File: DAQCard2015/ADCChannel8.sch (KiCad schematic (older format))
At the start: 50 parts, among them U10 LTC6403, U6 LTC6403, U7 AD9219, U8 LTC6403, U9 LTC6403

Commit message: Replaces single ample with 4-channel varients. Greatly reducing part count
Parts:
- removed C23, C33, C37, C38: .01uF, symbol C
- removed C24, C25, C29, C31, C32: .1uF, symbol C
- removed C26, C27, C28, C34, C35, C36, C39, C40, C41: C, symbol C
- removed C30: 2.2uF, symbol CP
- removed R25: Rt, symbol R
- removed R26, R27, R39, R40, R41, R42: Ri, symbol R
- removed R29, R30, R43, R44, R45, R46: Rf, symbol R
- removed R31: 10k, symbol R
- removed R47: 2.7k, symbol R
- removed R48: 1k, symbol R
- removed U10, U6, U8, U9: LTC6403, symbol LTC6403
- removed U7: AD9219, symbol AD9219
- added C45: .01uF, symbol C
- added C46, C47, C48, C50, C51: .1uF, symbol C
- added C49: 2.2uF, symbol CP
- added RP13: R_PACK8, symbol R_PACK8
- added RP14, RP15: Rf, symbol R_PACK4
- added U10: THS4524IDBTR, symbol THS4524IDBTR
- added U11: AD9219, symbol AD9219
- R33, R34: value Ri -> Rt
- R35: value Rf -> Rt
- R36: value Rf -> 2.7k
- R37: value Rt -> 1k
- R38: value Rt -> 10k
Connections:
- net labels added: 3V3ana, VOCM
- net labels removed: 18ana, 3V3, Vocm
- wire segments 178 -> 192
- no-connect marks 12 -> 4
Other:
- note removed: "100R Termination \nis common for all ADCs."

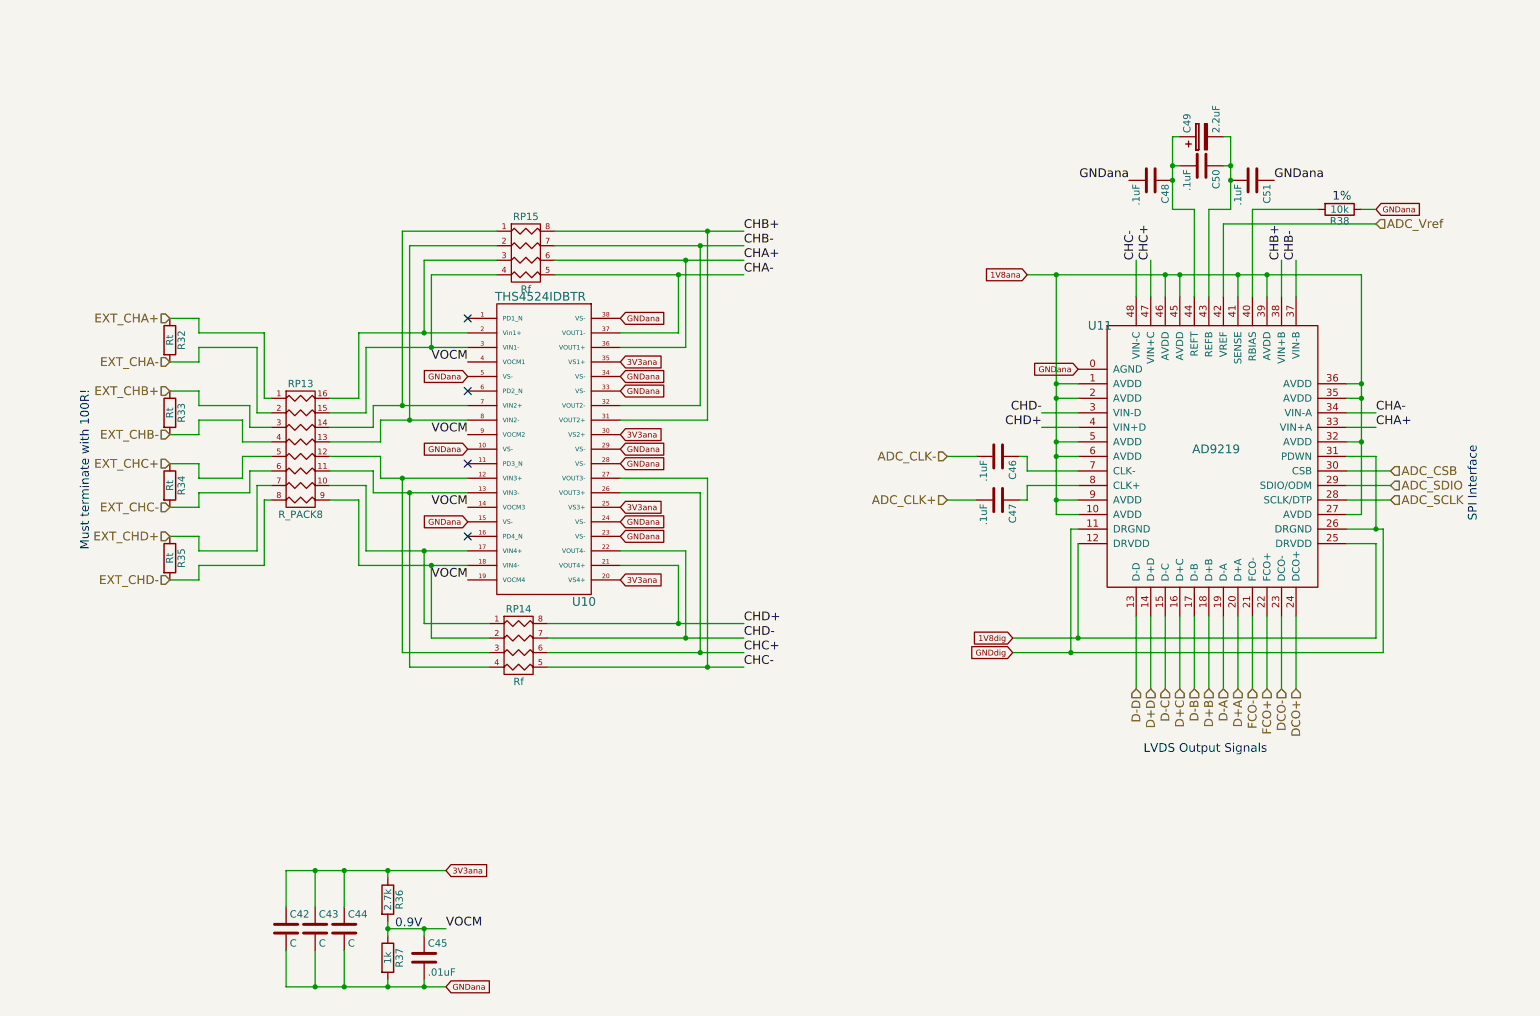
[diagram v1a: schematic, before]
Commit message: Finishes initial version of schematic(mostly). And adds a whole bunch of new footprints!
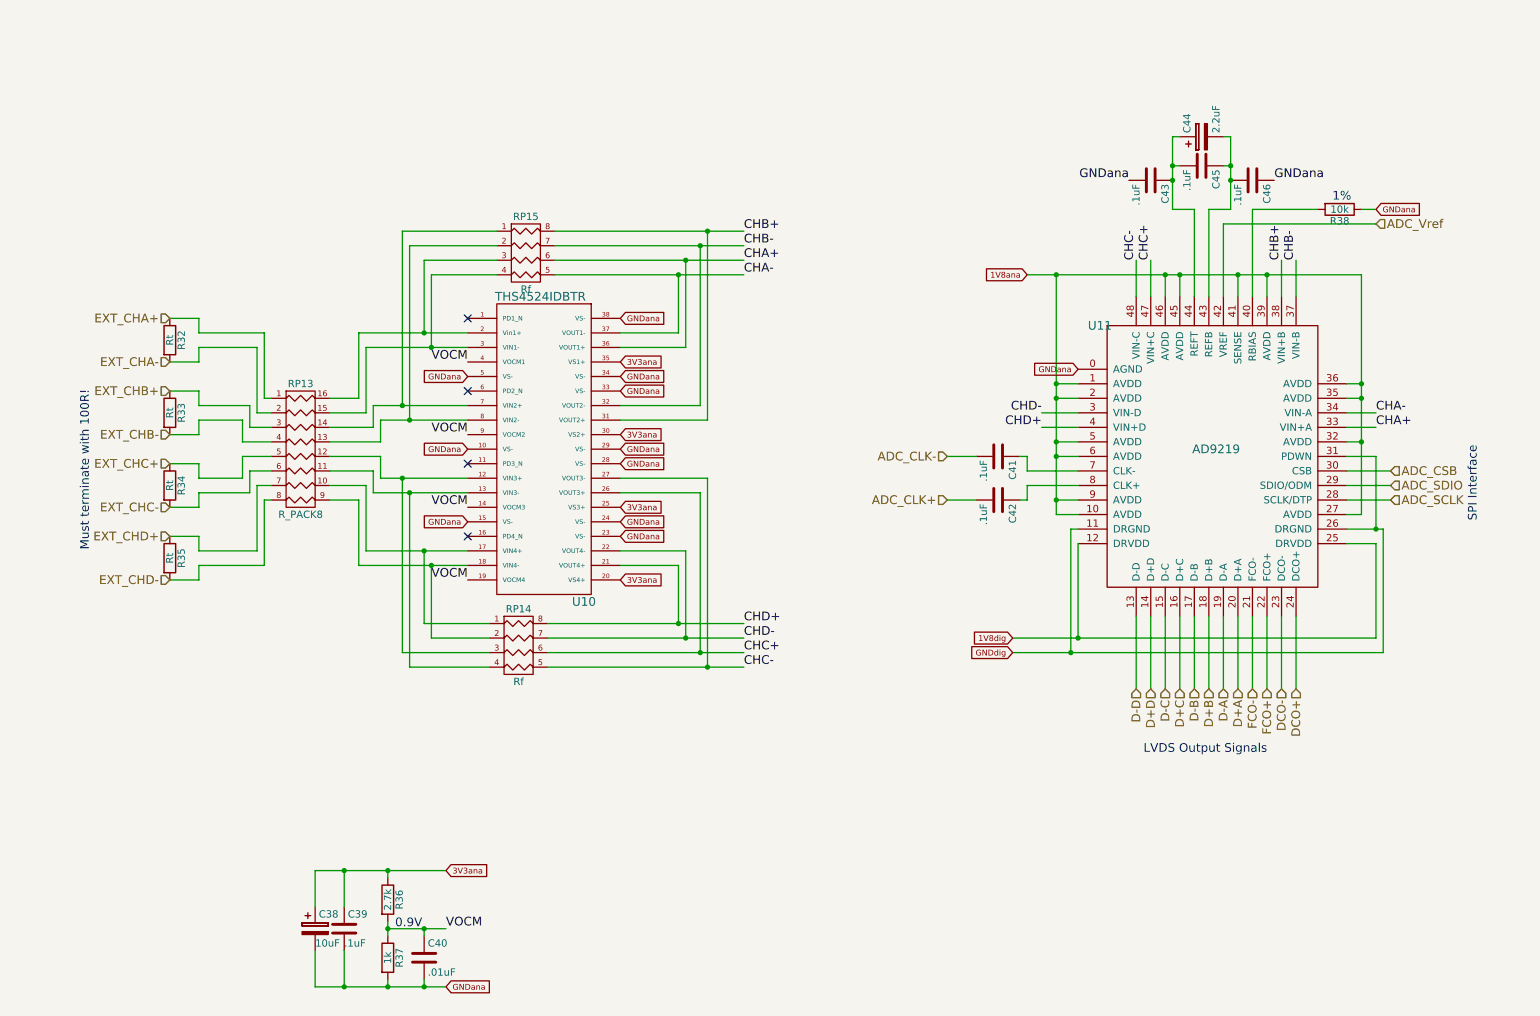
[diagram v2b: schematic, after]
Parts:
- removed C44: C, symbol C
- removed C47, C48, C50, C51: .1uF, symbol C
- removed C49: 2.2uF, symbol CP
- added C38: 10uF, extras:SMD_Cap_3mmDia, symbol CP
- added C39, C41: .1uF, Capacitors_SMD:C_0603, symbol C
- added C40: .01uF, Capacitors_SMD:C_0603, symbol C
- added C44: 2.2uF, extras:SMD_Cap_3mmDia, symbol CP
- C42, C43: value C -> .1uF; footprint (none) -> Capacitors_SMD:C_0603
- C45: value .01uF -> .1uF; footprint (none) -> Capacitors_SMD:C_0603
- C46: footprint (none) -> Capacitors_SMD:C_0603
- R32, R33, R34, R35, R36, R37, R38: footprint (none) -> Resistors_SMD:R_0603
- RP13: footprint (none) -> extras:R8_MNR18
- RP14, RP15: footprint (none) -> extras:R4-MNR04
- U10: footprint (none) -> Housings_SSOP:TSSOP-38_4.4x9.7mm_Pitch0.5mm
- U11: footprint (none) -> SMD_Packages:QFN-48-1EP
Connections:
- net 3V3ana: now also C38.1, C39.1; no longer C42.1, C43.1
- net ADC_CLK+: now also C42.2
- net ADC_CLK-: now also C41.2; no longer C46.2
- net GNDana: now also C46.1, C38.2, C39.2, C40.2; no longer C42.2, C45.2
- net VOCM: now also C40.1; no longer C45.1
- net at U11.43 (REFB): now also C45.1, C46.2, C44.2
- net at U11.44 (REFT): now also C43.1, C45.2, C44.1
- net at U11.7 (CLK-): now also C41.1; no longer C46.1
- net at U11.8 (CLK+): now also C42.1
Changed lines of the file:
@@
 $Comp
 L AD9219 U11
-U 1 1 55CFF5AF
+U 1 1 55CB5754
 P 9050 3700
 F 0 "U11" H 8250 4650 60  0000 C CNN
 F 1 "AD9219" H 9050 3800 60  0000 C CNN
-F 2 "" H 8650 3700 60  0000 C CNN
+F 2 "SMD_Packages:QFN-48-1EP" H 8650 3700 60  0001 C CNN
 F 3 "" H 8650 3700 60  0000 C CNN
 	1    9050 3700
@@
 $Comp
 L R R36
-U 1 1 55CFF5F1
+U 1 1 55CB5785
 P 3350 6700
 F 0 "R36" V 3430 6700 50  0000 C CNN
 F 1 "2.7k" V 3350 6700 50  0000 C CNN
-F 2 "" V 3280 6700 30  0000 C CNN
+F 2 "Resistors_SMD:R_0603" V 3280 6700 30  0001 C CNN
 F 3 "" H 3350 6700 30  0000 C CNN
 	1    3350 6700
@@
 $Comp
 L R R37
-U 1 1 55CE4056
+U 1 1 55CB5779
 P 3350 7100
 F 0 "R37" V 3430 7100 50  0000 C CNN
 F 1 "1k" V 3350 7100 50  0000 C CNN
-F 2 "" V 3280 7100 30  0000 C CNN
+F 2 "Resistors_SMD:R_0603" V 3280 7100 30  0001 C CNN
 F 3 "" H 3350 7100 30  0000 C CNN
 	1    3350 7100
@@
 Must terminate with 100R!
 $Comp
-L C C42
-U 1 1 55CFF5CC
-P 2650 6900
-F 0 "C42" H 2675 7000 50  0000 L CNN
-F 1 "C" H 2675 6800 50  0000 L CNN
-F 2 "" H 2688 6750 30  0000 C CNN
-F 3 "" H 2650 6900 60  0000 C CNN
-	1    2650 6900
-	1    0    0    -1
-$EndComp
-$Comp
-L C C43
-U 1 1 55CFF5B7
-P 2850 6900
-F 0 "C43" H 2875 7000 50  0000 L CNN
-F 1 "C" H 2875 6800 50  0000 L CNN
-F 2 "" H 2888 6750 30  0000 C CNN
-F 3 "" H 2850 6900 60  0000 C CNN
-	1    2850 6900
-	1    0    0    -1
-$EndComp
-$Comp
-L C C44
-U 1 1 55CFF5BF
+L C C39
+U 1 1 55CB575A
 P 3050 6900
-F 0 "C44" H 3075 7000 50  0000 L CNN
-F 1 "C" H 3075 6800 50  0000 L CNN
-F 2 "" H 3088 6750 30  0000 C CNN
+F 0 "C39" H 3075 7000 50  0000 L CNN
+F 1 ".1uF" H 3050 6800 50  0000 L CNN
+F 2 "Capacitors_SMD:C_0603" H 3088 6750 30  0001 C CNN
 F 3 "" H 3050 6900 60  0000 C CNN
 	1    3050 6900
@@
 ADC_SCLK
 $Comp
-L C C46
-U 1 1 55CFF5C4
+L C C41
+U 1 1 55CB5763
 P 7550 3650
-F 0 "C46" H 7575 3750 50  0000 L CNN
+F 0 "C41" H 7575 3750 50  0000 L CNN
 F 1 ".1uF" H 7575 3550 50  0000 L CNN
-F 2 "" H 7588 3500 30  0000 C CNN
+F 2 "Capacitors_SMD:C_0603" H 7588 3500 30  0001 C CNN
 F 3 "" H 7550 3650 60  0000 C CNN
 	1    7550 3650
@@
 $EndComp
 $Comp
-L C C47
-U 1 1 55CFF5E4
+L C C42
+U 1 1 55CB5748
 P 7550 3950
-F 0 "C47" H 7575 4050 50  0000 L CNN
+F 0 "C42" H 7575 4050 50  0000 L CNN
 F 1 ".1uF" H 7575 3850 50  0000 L CNN
-F 2 "" H 7588 3800 30  0000 C CNN
+F 2 "Capacitors_SMD:C_0603" H 7588 3800 30  0001 C CNN
 F 3 "" H 7550 3950 60  0000 C CNN
 	1    7550 3950
@@
 DCO+
 $Comp
-L C C51
-U 1 1 55CFF5FA
+L C C46
+U 1 1 55CFF5FE
 P 9300 1750
-F 0 "C51" H 9325 1850 50  0000 L CNN
+F 0 "C46" H 9325 1850 50  0000 L CNN
 F 1 ".1uF" H 9325 1650 50  0000 L CNN
-F 2 "" H 9338 1600 30  0000 C CNN
+F 2 "Capacitors_SMD:C_0603" H 9338 1600 30  0001 C CNN
 F 3 "" H 9300 1750 60  0000 C CNN
 	1    9300 1750
@@
 $EndComp
 $Comp
-L C C48
-U 1 1 55CFF5CF
+L C C43
+U 1 1 55CB5769
 P 8600 1750
-F 0 "C48" H 8625 1850 50  0000 L CNN
+F 0 "C43" H 8625 1850 50  0000 L CNN
 F 1 ".1uF" H 8625 1650 50  0000 L CNN
-F 2 "" H 8638 1600 30  0000 C CNN
+F 2 "Capacitors_SMD:C_0603" H 8638 1600 30  0001 C CNN
 F 3 "" H 8600 1750 60  0000 C CNN
 	1    8600 1750
@@
 $EndComp
 $Comp
-L C C50
-U 1 1 55CFF5DB
+L C C45
+U 1 1 55CB5774
 P 8950 1650
-F 0 "C50" H 8975 1750 50  0000 L CNN
+F 0 "C45" H 8975 1750 50  0000 L CNN
 F 1 ".1uF" H 8975 1550 50  0000 L CNN
-F 2 "" H 8988 1500 30  0000 C CNN
+F 2 "Capacitors_SMD:C_0603" H 8988 1500 30  0001 C CNN
 F 3 "" H 8950 1650 60  0000 C CNN
 	1    8950 1650
@@
 GNDana
 $Comp
-L CP C49
-U 1 1 55CFF603
+L CP C44
+U 1 1 55CB5793
 P 8950 1450
-F 0 "C49" H 8975 1550 50  0000 L CNN
+F 0 "C44" H 8975 1550 50  0000 L CNN
 F 1 "2.2uF" H 8975 1350 50  0000 L CNN
-F 2 "" H 8988 1300 30  0000 C CNN
+F 2 "extras:SMD_Cap_3mmDia" H 8988 1300 30  0001 C CNN
 F 3 "" H 8950 1450 60  0000 C CNN
 	1    8950 1450
@@
 $Comp
 L R R38
-U 1 1 55CE40D3
+U 1 1 55CFF5ED
 P 9900 1950
 F 0 "R38" V 9980 1950 50  0000 C CNN
 F 1 "10k" V 9900 1950 50  0000 C CNN
-F 2 "" V 9830 1950 30  0000 C CNN
+F 2 "Resistors_SMD:R_0603" V 9830 1950 30  0001 C CNN
 F 3 "" H 9900 1950 30  0000 C CNN
 	1    9900 1950
@@
 $Comp
 L THS4524IDBTR U10
-U 1 1 55CFF608
+U 1 1 55CB579B
 P 4400 3700
 F 0 "U10" H 4700 2750 60  0000 C CNN
 F 1 "THS4524IDBTR" H 4400 4850 60  0000 C CNN
-F 2 "" H 4600 3800 60  0000 C CNN
+F 2 "Housings_SSOP:TSSOP-38_4.4x9.7mm_Pitch0.5mm" H 4600 3800 60  0001 C CNN
 F 3 "" H 4600 3800 60  0000 C CNN
 	1    4400 3700
@@
 $EndComp
 $Comp
-L C C45
-U 1 1 55CFF612
+L C C40
+U 1 1 55CB57A2
 P 3600 7100
-F 0 "C45" H 3625 7200 50  0000 L CNN
+F 0 "C40" H 3625 7200 50  0000 L CNN
 F 1 ".01uF" H 3625 7000 50  0000 L CNN
-F 2 "" H 3638 6950 30  0000 C CNN
+F 2 "Capacitors_SMD:C_0603" H 3638 6950 30  0001 C CNN
 F 3 "" H 3600 7100 60  0000 C CNN
 	1    3600 7100
@@
 Connection ~ 3600 6900
 Wire Wire Line
-	2650 6500 3750 6500
-Wire Wire Line
 	3050 6500 3050 6750
 Connection ~ 3350 6500
@@
 Connection ~ 3050 6500
 Wire Wire Line
-	2650 6500 2650 6750
-Connection ~ 2850 6500
-Wire Wire Line
-	2650 7300 3750 7300
-Wire Wire Line
 	3050 7300 3050 7050
 Wire Wire Line
 	2850 7300 2850 7050
 Connection ~ 3050 7300
-Wire Wire Line
-	2650 7300 2650 7050
-Connection ~ 2850 7300
 Wire Wire Line
 	3600 7300 3600 7250
@@
 $Comp
 L R R35
-U 1 1 55CFF619
+U 1 1 55CFF61A
 P 1850 4350
 F 0 "R35" V 1930 4350 50  0000 C CNN
 F 1 "Rt" V 1850 4350 50  0000 C CNN
-F 2 "" V 1780 4350 30  0000 C CNN
+F 2 "Resistors_SMD:R_0603" V 1780 4350 30  0001 C CNN
 F 3 "" H 1850 4350 30  0000 C CNN
 	1    1850 4350
@@
 $Comp
 L R R34
-U 1 1 55CFF61C
+U 1 1 55CB57B3
 P 1850 3850
 F 0 "R34" V 1930 3850 50  0000 C CNN
 F 1 "Rt" V 1850 3850 50  0000 C CNN
-F 2 "" V 1780 3850 30  0000 C CNN
+F 2 "Resistors_SMD:R_0603" V 1780 3850 30  0001 C CNN
 F 3 "" H 1850 3850 30  0000 C CNN
 	1    1850 3850
@@
 $Comp
 L R R33
-U 1 1 55CFF625
+U 1 1 55CB57B6
 P 1850 3350
 F 0 "R33" V 1930 3350 50  0000 C CNN
 F 1 "Rt" V 1850 3350 50  0000 C CNN
-F 2 "" V 1780 3350 30  0000 C CNN
+F 2 "Resistors_SMD:R_0603" V 1780 3350 30  0001 C CNN
 F 3 "" H 1850 3350 30  0000 C CNN
 	1    1850 3350
@@
 $Comp
 L R R32
-U 1 1 55CFF62A
+U 1 1 55CB57C0
 P 1850 2850
 F 0 "R32" V 1930 2850 50  0000 C CNN
 F 1 "Rt" V 1850 2850 50  0000 C CNN
-F 2 "" V 1780 2850 30  0000 C CNN
+F 2 "Resistors_SMD:R_0603" V 1780 2850 30  0001 C CNN
 F 3 "" H 1850 2850 30  0000 C CNN
 	1    1850 2850
@@
 $Comp
 L R_PACK4 RP14
-U 1 1 55CFF636
+U 1 1 55CB57C9
 P 4250 5150
 F 0 "RP14" H 4250 5600 50  0000 C CNN
 F 1 "Rf" H 4250 5100 50  0000 C CNN
-F 2 "" H 4250 5150 60  0000 C CNN
+F 2 "extras:R4-MNR04" H 4250 5150 60  0001 C CNN
 F 3 "" H 4250 5150 60  0000 C CNN
 	1    4250 5150
@@
 $Comp
 L R_PACK4 RP15
-U 1 1 55CFF63A
+U 1 1 55CB574D
 P 4300 2450
 F 0 "RP15" H 4300 2900 50  0000 C CNN
 F 1 "Rf" H 4300 2400 50  0000 C CNN
-F 2 "" H 4300 2450 60  0000 C CNN
+F 2 "extras:R4-MNR04" H 4300 2450 60  0001 C CNN
 F 3 "" H 4300 2450 60  0000 C CNN
 	1    4300 2450
@@
 $Comp
 L R_PACK8 RP13
-U 1 1 55CFF642
+U 1 1 55CB57CE
 P 2750 3600
 F 0 "RP13" H 2750 4050 50  0000 C CNN
 F 1 "R_PACK8" H 2750 3150 50  0000 C CNN
-F 2 "" H 2750 3600 60  0000 C CNN
+F 2 "extras:R8_MNR18" H 2750 3600 60  0001 C CNN
 F 3 "" H 2750 3600 60  0000 C CNN
 	1    2750 3600
@@
 Text GLabel 10150 1950 2    40   Input ~ 0
 GNDana
+Wire Wire Line
+	3750 6500 2850 6500
+Wire Wire Line
+	2850 7300 3750 7300
+$Comp
+L CP C38
+U 1 1 55CB5740
+P 2850 6900
+F 0 "C38" H 2875 7000 50  0000 L CNN
+F 1 "10uF" H 2850 6800 50  0000 L CNN
+F 2 "extras:SMD_Cap_3mmDia" H 2888 6750 30  0001 C CNN
+F 3 "" H 2850 6900 60  0000 C CNN
+	1    2850 6900
+	1    0    0    -1
+$EndComp
 $EndSCHEMATC

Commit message: Adds a more-or-less complete BOM to DAQ Card
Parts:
- C40: value .01uF -> 10000pF
- RP13: value R_PACK8 -> Ri
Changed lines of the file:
@@
 $Descr A4 11693 8268
 encoding utf-8
-Sheet 3 13
+Sheet 7 13
 Title ""
 Date ""
@@
 P 3600 7100
 F 0 "C40" H 3625 7200 50  0000 L CNN
-F 1 ".01uF" H 3625 7000 50  0000 L CNN
+F 1 "10000pF" H 3625 7000 50  0000 L CNN
 F 2 "Capacitors_SMD:C_0603" H 3638 6950 30  0001 C CNN
 F 3 "" H 3600 7100 60  0000 C CNN
@@
 P 2750 3600
 F 0 "RP13" H 2750 4050 50  0000 C CNN
-F 1 "R_PACK8" H 2750 3150 50  0000 C CNN
+F 1 "Ri" H 2750 3150 50  0000 C CNN
 F 2 "extras:R8_MNR18" H 2750 3600 60  0001 C CNN
 F 3 "" H 2750 3600 60  0000 C CNN

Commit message: Updates to DAQCard2015, especially to power systems
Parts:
- C38, C44: footprint extras:SMD_Cap_3mmDia -> Capacitors_SMD:C_0805
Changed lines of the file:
@@
 F 0 "C44" H 8975 1550 50  0000 L CNN
 F 1 "2.2uF" H 8975 1350 50  0000 L CNN
-F 2 "extras:SMD_Cap_3mmDia" H 8988 1300 30  0001 C CNN
+F 2 "Capacitors_SMD:C_0805" H 8988 1300 30  0001 C CNN
 F 3 "" H 8950 1450 60  0000 C CNN
 	1    8950 1450
@@
 F 0 "C38" H 2875 7000 50  0000 L CNN
 F 1 "10uF" H 2850 6800 50  0000 L CNN
-F 2 "extras:SMD_Cap_3mmDia" H 2888 6750 30  0001 C CNN
+F 2 "Capacitors_SMD:C_0805" H 2888 6750 30  0001 C CNN
 F 3 "" H 2850 6900 60  0000 C CNN
 	1    2850 6900
